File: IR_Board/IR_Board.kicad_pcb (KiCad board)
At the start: 2 copper layers, 189.9 x 157.6 mm, 71 parts, among them J1 Conn_02x08_Top_Bottom, Q1 FDG6335N, Q10 FDG6335N, Q11 FDG6335N, Q12 FDG6335N, Q13 FDG6335N, Q14 FDG6335N, Q2 FDG6335N, Q3 FDG6335N, Q4 FDG6335N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

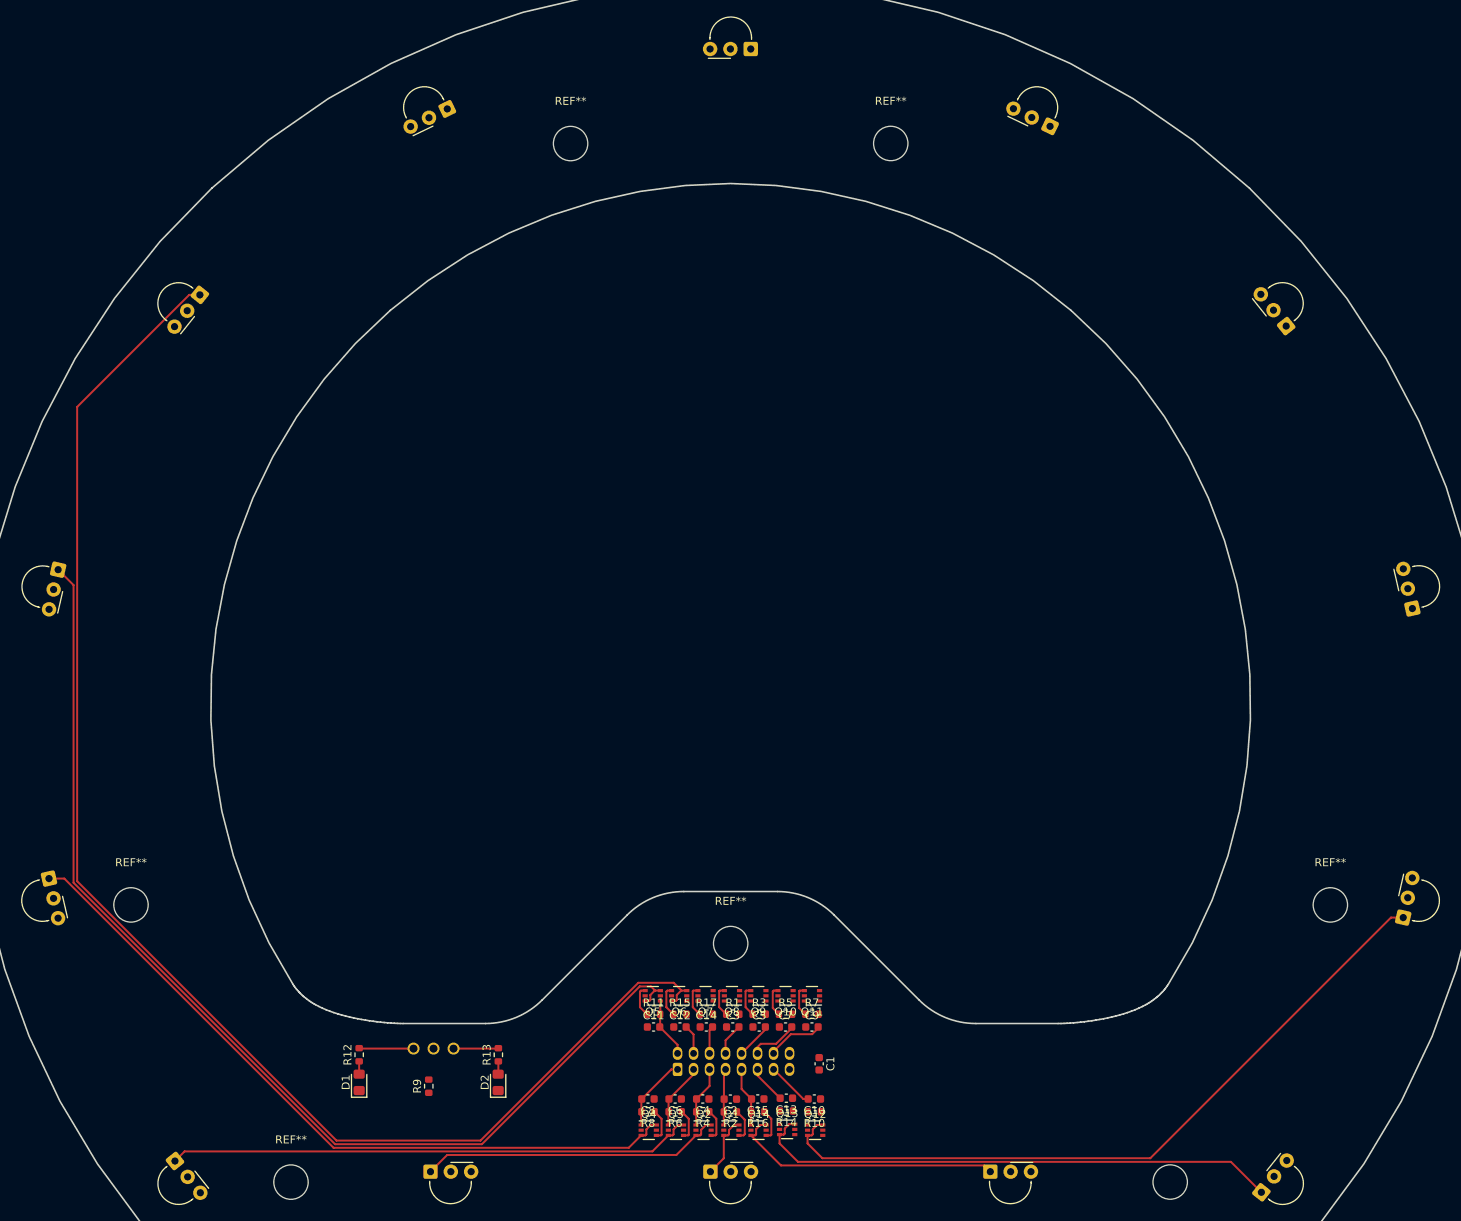
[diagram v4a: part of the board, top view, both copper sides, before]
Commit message: Continued drawing traces [IR BOARD]
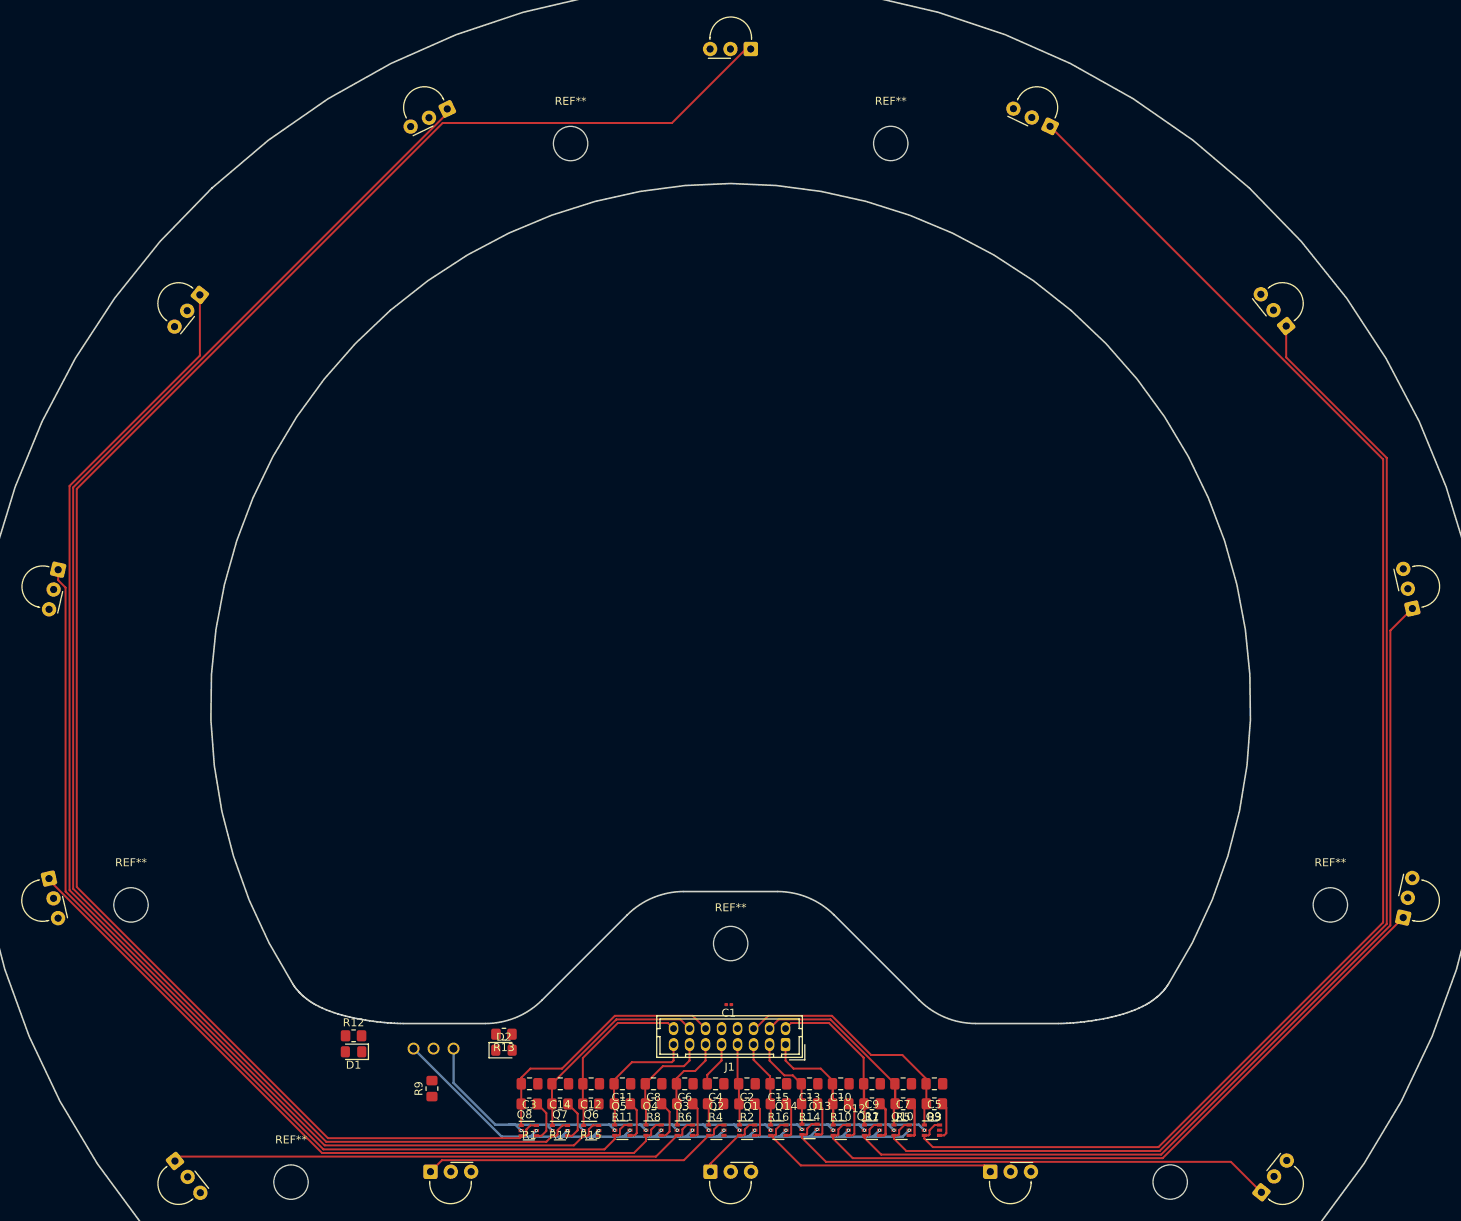
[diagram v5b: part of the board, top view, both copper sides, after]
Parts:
- removed the REF** at (151.4, 134.9)
- added REF**: MountingHole_4.3mm_M4_ISO14580, MountingHole:MountingHole_4.3mm_M4_ISO14580, F.Cu at (151.4, 134.9)
- C1: footprint Capacitor_SMD:C_0603_1608Metric -> Capacitor_SMD:C_0201_0603Metric
- C10, C11, C12, C13, C14, C15, C2, C3, C4, C5, C6, C7, C8, C9: footprint Capacitor_SMD:C_0603_1608Metric -> Capacitor_SMD:C_0805_2012Metric_Pad1.18x1.45mm_HandSolder
- J1: value Conn_02x08_Top_Bottom -> CONN_OUT; moved to F.Cu
- R1, R10, R11, R12, R13, R14, R15, R16, R17, R2, R3, R4, R5, R6, R7, R8, R9: footprint Resistor_SMD:R_0603_1608Metric -> Resistor_SMD:R_0805_2012Metric_Pad1.20x1.40mm_HandSolder
- moved Q8 30.5 mm to (126.2, 158.2), turned to 0 degrees
- moved R1 27.8 mm to (126.3, 154.9), turned to 180 degrees
- moved Q9 27.4 mm to (176.6, 158.2), turned to 0 degrees
- moved C3 26.4 mm to (126.3, 152.4), turned to 180 degrees
- moved Q7 24.8 mm to (130.1, 158.2), turned to 0 degrees
- moved R3 24.6 mm to (176.9, 154.9), turned to 180 degrees
- moved C5 23.0 mm to (176.9, 152.4), turned to 180 degrees
- moved Q10 22.2 mm to (172.8, 158.2), turned to 0 degrees
- moved R17 21.5 mm to (130.1, 154.9), turned to 180 degrees
- moved Q6 20.1 mm to (134.0, 158.2), turned to 0 degrees
- moved C14 19.6 mm to (130.1, 152.4), turned to 180 degrees
- moved R5 18.5 mm to (173.0, 154.9), turned to 180 degrees
- moved Q11 18.4 mm to (169.1, 158.2), turned to 0 degrees
- moved Q5 17.2 mm to (137.9, 158.2), turned to 0 degrees
- moved C7 16.3 mm to (173.0, 152.4), turned to 180 degrees
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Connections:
- J1 pad 1: IR4 -> IR12
- J1 pad 10: IR9 -> +3V3
- J1 pad 11: IR13 -> IR3
- J1 pad 12: IR10 -> IR8
- J1 pad 13: IR12 -> IR4
- J1 pad 14: IR11 -> IR7
- J1 pad 15: +3V3 -> IR5
- J1 pad 16: GND -> IR6
- J1 pad 2: IR5 -> IR11
- J1 pad 3: IR3 -> IR13
- J1 pad 4: IR6 -> IR10
- J1 pad 5: IR2 -> IR14
- J1 pad 6: IR7 -> IR9
- J1 pad 8: IR8 -> GND
- J1 pad 9: IR14 -> IR2
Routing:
- net Net-(Q8-Pad3): track 0.00 -> 228.4 mm
- net Net-(Q7-Pad3): track 0.00 -> 192.9 mm
- net Net-(Q9-Pad3): track 0.00 -> 189.3 mm
- net Net-(Q10-Pad3): track 0.00 -> 157.1 mm
- net Net-(Q11-Pad3): track 0.00 -> 122.3 mm
- net A: track 5.62 -> 79.2 mm, vias 0 -> 14
- net B: track 6.82 -> 80.3 mm, vias 0 -> 13
- net IR8: track 3.99 -> 32.9 mm
- net IR9: track 4.53 -> 31.4 mm
- net IR7: track 3.46 -> 26.2 mm
- net Net-(Q6-Pad3): track 180.8 -> 162.0 mm
- net IR10: track 6.26 -> 24.7 mm
- net IR6: track 3.68 -> 21.9 mm
- net IR11: track 7.23 -> 20.3 mm
- net Net-(Q5-Pad3): track 137.4 -> 126.4 mm
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
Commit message: Finished IR, generated gerbers, ordered designs
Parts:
- added REF**: OSHW-Logo2_9.8x8mm_SilkScreen, Symbol:OSHW-Logo2_9.8x8mm_SilkScreen, B.Cu at (138.8, 166.0)
- added REF**: KiCad-Logo2_5mm_SilkScreen, Symbol:KiCad-Logo2_5mm_SilkScreen, B.Cu at (167.2, 166.5)
- moved R9 0.20 mm to (114.3, 153.0)
- renumbered REF** to MH
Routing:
- net B: track 80.3 -> 92.4 mm, vias 13 -> 14
- net A: track 79.2 -> 85.3 mm
- net +3V3: track 0.00 -> 5.18 mm, vias 0 -> 1
- net Net-(Q2-Pad4): track 0.00 -> 4.97 mm
- net Net-(Q6-Pad4): track 0.00 -> 4.85 mm
- net Net-(Q8-Pad3): track 228.4 -> 231.0 mm
- net IR2: track 8.35 -> 10.9 mm
- net Net-(D2-Pad2): track 0.00 -> 2.01 mm
- net Net-(D1-Pad2): track 0.00 -> 2.01 mm
- net GND: vias 0 -> 14
- added copper zone on B.Cu, net +3V3
- added copper zone on B.Cu, net GND
- added copper zone on F.Cu, net GND
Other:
- board text added: "IR Sensor Board Designed by Pixeljoch Funded by Leaphy"
- board text added: "also available in (infra)red"
- board text added: "if you can see this you're probably cheating"
- board text added: "not for use in visible light"
